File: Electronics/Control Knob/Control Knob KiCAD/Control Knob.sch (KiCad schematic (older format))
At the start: 3 parts, among them J1 Knob Connector, SW1 Switch

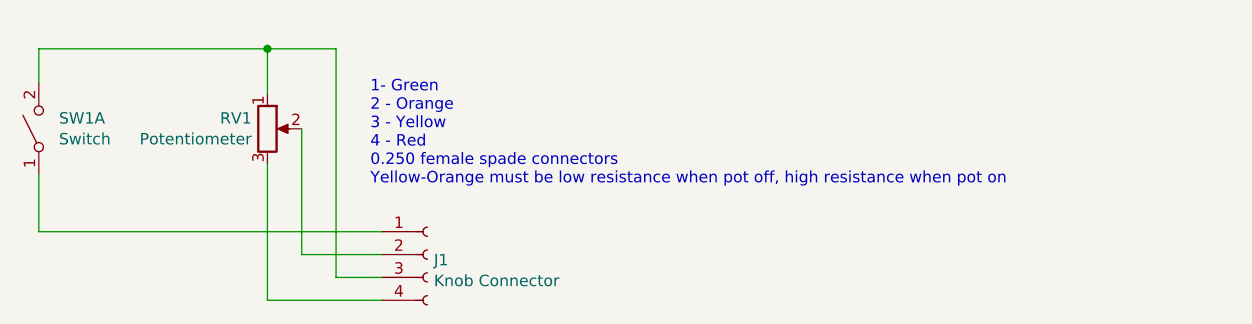
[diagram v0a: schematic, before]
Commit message: Fixed mistake in control knob schematic.
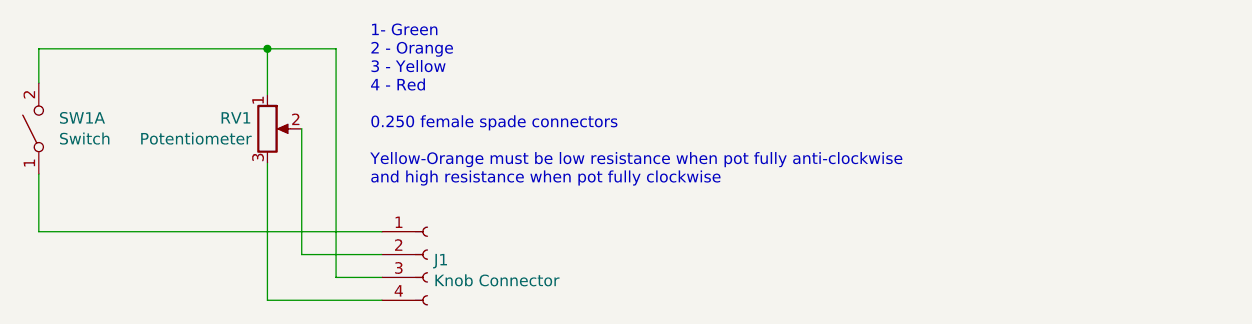
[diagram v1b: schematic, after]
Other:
- note added: "1- Green\n2 - Orange\n3 - Yellow\n4 - Red\n\n0.250 female spade connectors\n\nYellow-Orange must be low resistance when pot fully anti-clockwise\nand high resistance when pot fully clockwise"
- note removed: "1- Green\n2 - Orange\n3 - Yellow\n4 - Red\n0.250 female spade connectors\nYellow-Orange must be low resistance when pot off, high resistance when pot on"
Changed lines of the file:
@@
 $EndComp
 Text Notes 5350 3750 0    50   ~ 0
-1- Green\n2 - Orange\n3 - Yellow\n4 - Red\n0.250 female spade connectors\nYellow-Orange must be low resistance when pot off, high resistance when pot on
+1- Green\n2 - Orange\n3 - Yellow\n4 - Red\n\n0.250 female spade connectors\n\nYellow-Orange must be low resistance when pot fully anti-clockwise\nand high resistance when pot fully clockwise
 Wire Wire Line
 	4900 3650 4900 4250
